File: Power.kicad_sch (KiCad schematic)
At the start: 54 parts, among them J2 Charge, J3 Battery, Q1 AO3401A, Q2 AO3400A, Q3 AO3401A, U4 FUSB303BTMX, U5 TPS61089, U6 D3V3XA4B10LP, U7 BQ25895RTW, U8 TPS63001

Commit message: Reset PCB
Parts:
- removed R20, R21, R22: 10k, Resistor_SMD:R_0603_1608Metric, symbol Device:R
- renumbered R23 to R20, R24 to R21, R25 to R22, R26 to R23, R27 to R24

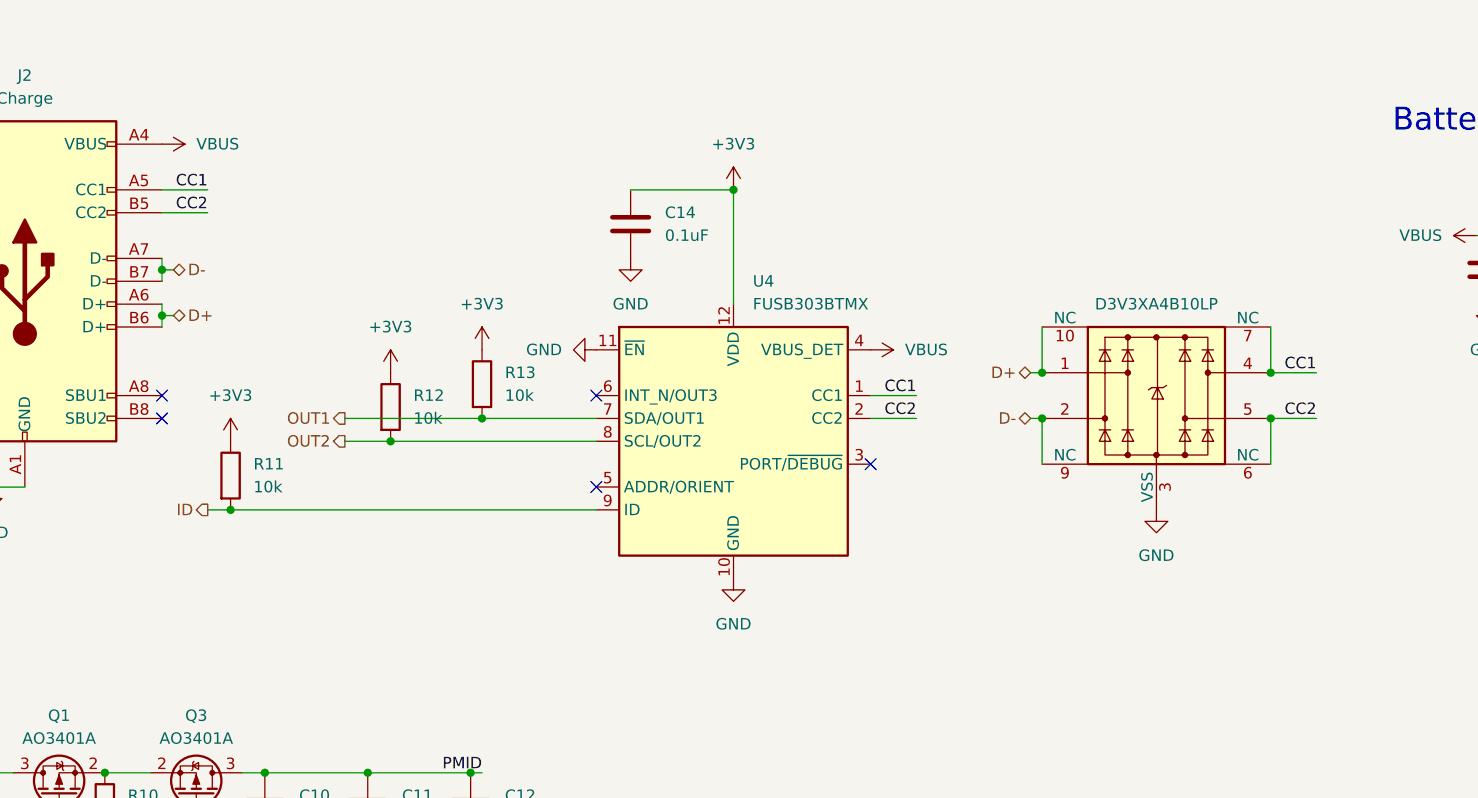
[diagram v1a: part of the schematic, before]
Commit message: Group power components
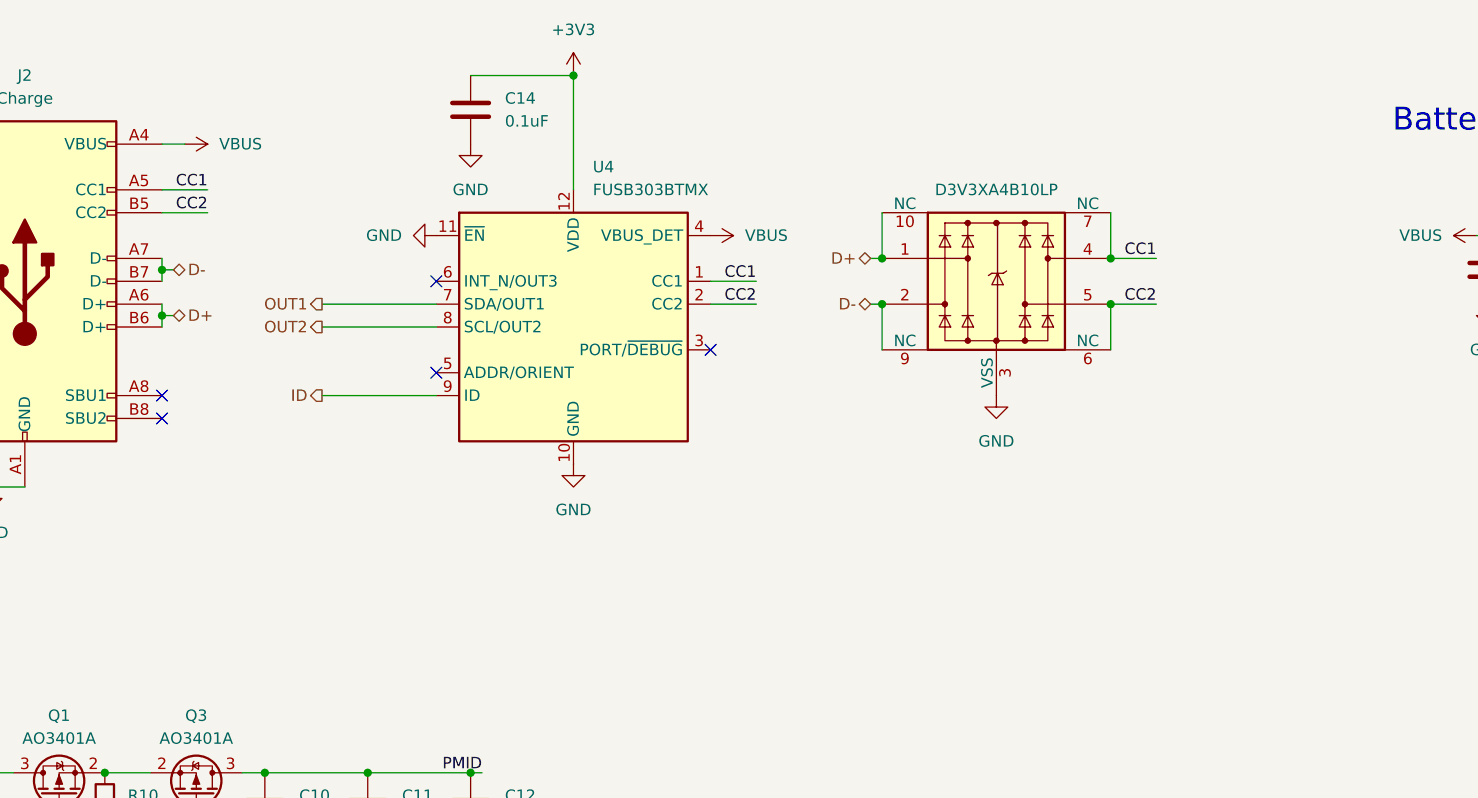
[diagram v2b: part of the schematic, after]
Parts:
- removed R11, R12, R13: 10k, Resistor_SMD:R_0603_1608Metric, symbol Device:R
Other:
- moved on the sheet: C14, U4

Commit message: Fully routed, no DRC errors
tysm Kevin :D
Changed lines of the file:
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@@
 		(in_pos_files yes)
 		(dnp no)
-		(fields_autoplaced yes)
 		(property "Reference" "R21"
 			(at 233.68 29.2099 0)
@@
 					(size 1.27 1.27)
 				)
-				(justify right)
+				(justify left)
 			)
 		)

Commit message: BQ fixes
i hate my life
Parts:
- added R26: 100R, Resistor_SMD:R_0603_1608Metric, symbol Device:R
- added TP1, TP2, TP3, TP4: TestPoint, TestPoint:TestPoint_Pad_D2.0mm, symbol Connector:TestPoint
- renumbered C14 to C12, C12 to C13, C13 to C14, R14 to R11, R15 to R12, R16 to R13, R17 to R14, R18 to R15, R19 to R16, R20 to R17, R21 to R18, R22 to R19, R23 to R20, R24 to R21
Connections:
- net +12V: now also TP2.1
- net +3V3: now also U8.10 (FB), TP3.1
- net +BATT: now also TP4.1
- net GND: now also R26.2
- net VBUS: now also TP1.1
- net at U7.10 (ILIM): now also R26.1
- no-connect marks 10 -> 8
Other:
- moved on the sheet: C25

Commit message: Fix more bugs
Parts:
- added C28: 10uF, Capacitor_SMD:C_0603_1608Metric, symbol Device:C
- added R17: 10k, Resistor_SMD:R_0603_1608Metric, symbol ScottoKeebs:Placeholder_Resistor
- added R18: 100k, Resistor_SMD:R_0603_1608Metric, symbol ScottoKeebs:Placeholder_Resistor
- renumbered C28 to C29, R26 to R19, R17 to R20, R18 to R21, R19 to R22, R20 to R23, R21 to R24
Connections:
- net +3V3: now also C28.1, R17.1; no longer U7.8 (OTG)
- net GND: now also C28.2, R18.2
- net ~{INT}: now also R17.2
- new net OTG: R18.1, U7.8 (OTG)
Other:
- moved on the sheet: TP3
